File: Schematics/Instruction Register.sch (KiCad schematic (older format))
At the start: 44 parts, among them U44 74F157, U45 74F157, U46 74F574, U47 74F157, U48 74F157, U49 74F574

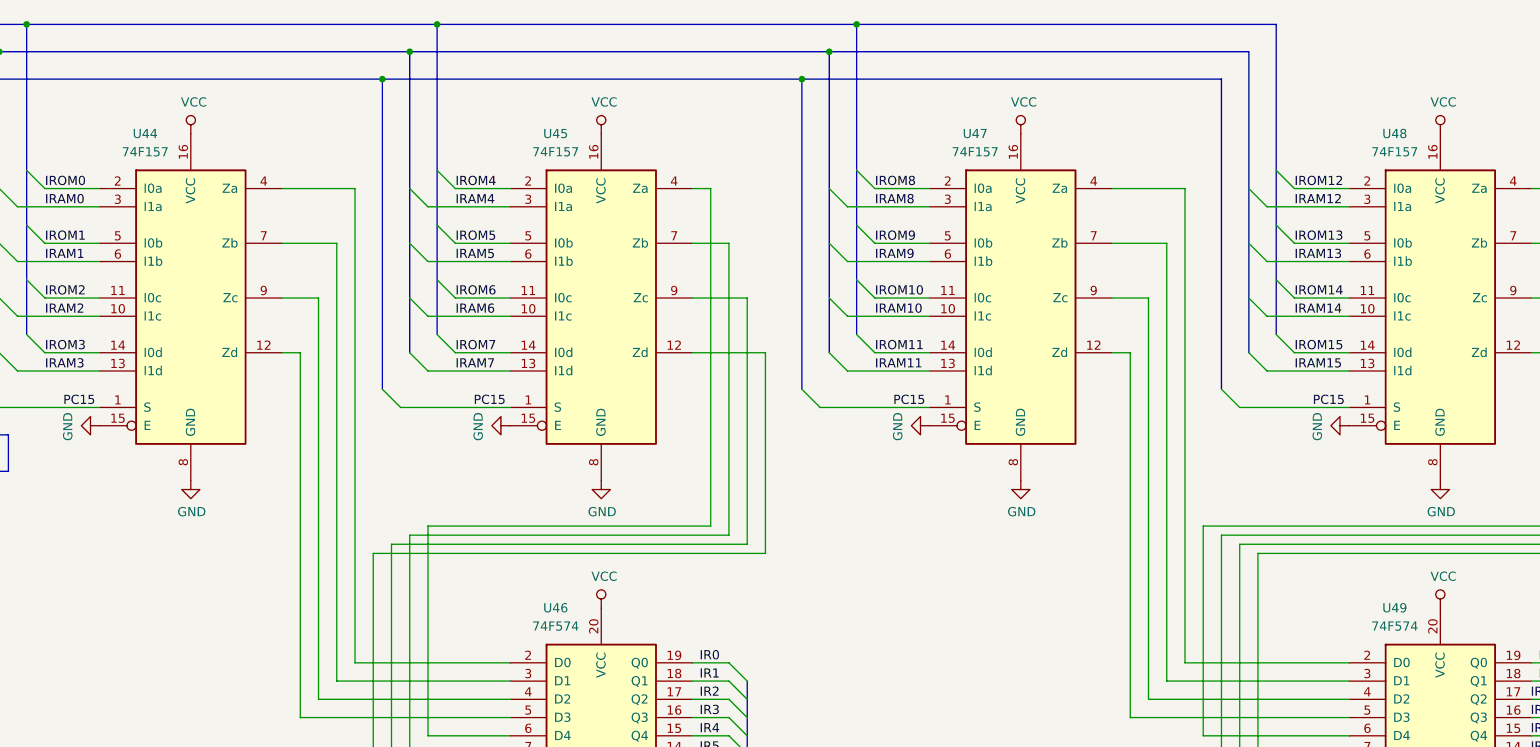
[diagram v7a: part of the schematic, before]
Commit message: Loosely group PCB footprints according to corresponding sheet.
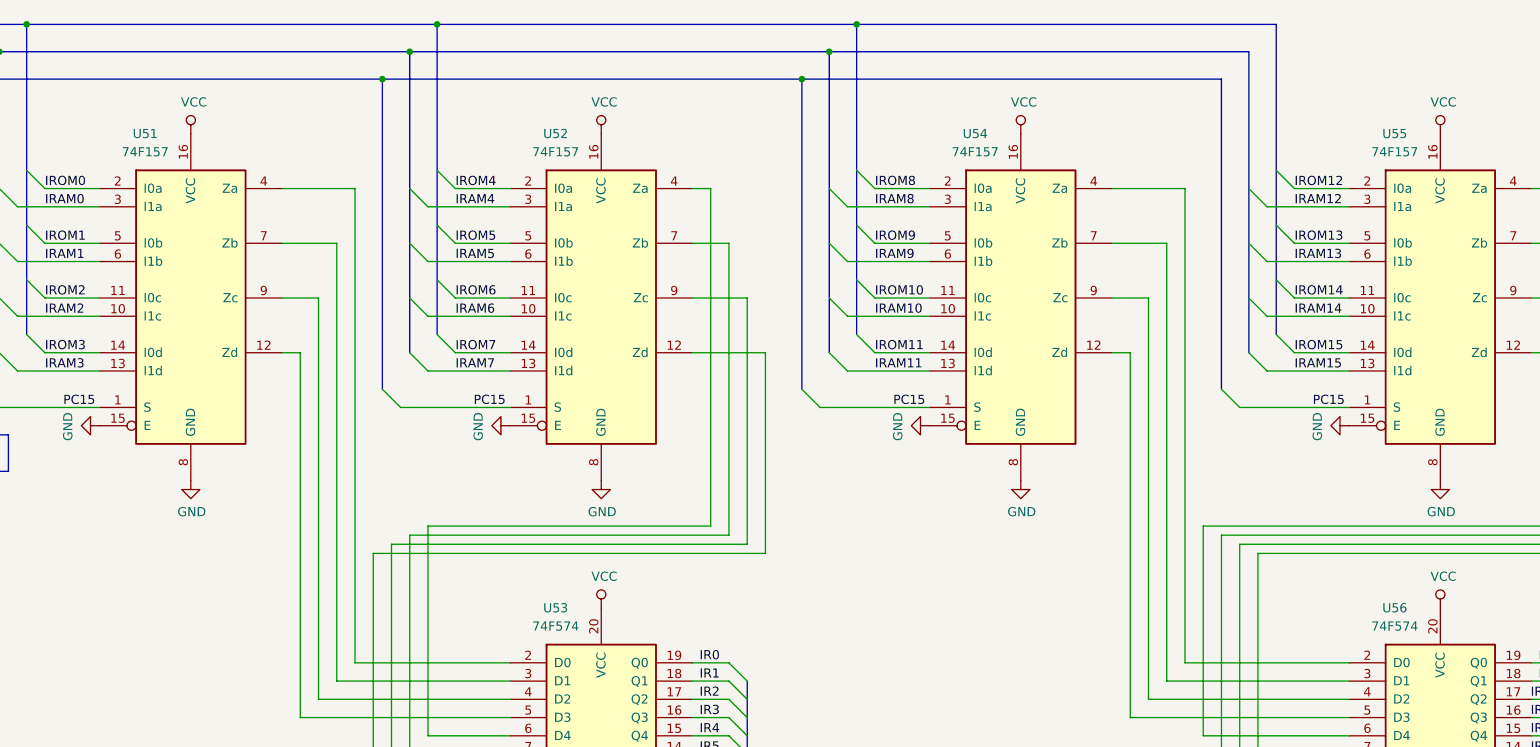
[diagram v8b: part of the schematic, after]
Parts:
- renumbered U44 to U51, U45 to U52, U46 to U53, U47 to U54, U48 to U55, U49 to U56
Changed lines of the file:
@@
 P 2100 2100
 AR Path="/5D2C14C3/5D23E2DA" Ref="U?"  Part="1"
-AR Path="/5D8005AF/5D833E49/5D23E2DA" Ref="U44"  Part="1"
-F 0 "U44" H 1850 3000 50  0000 C CNN
+AR Path="/5D8005AF/5D833E49/5D23E2DA" Ref="U51"  Part="1"
+F 0 "U51" H 1850 3000 50  0000 C CNN
 F 1 "74F157" H 1850 2900 50  0000 C CNN
 F 2 "Package_DIP:DIP-16_W7.62mm" H 2100 2100 50  0001 C CNN
@@
 P 4350 4600
 AR Path="/5D2C14C3/5D25C885" Ref="U?"  Part="1"
-AR Path="/5D8005AF/5D833E49/5D25C885" Ref="U46"  Part="1"
-F 0 "U46" H 4100 5400 50  0000 C CNN
+AR Path="/5D8005AF/5D833E49/5D25C885" Ref="U53"  Part="1"
+F 0 "U53" H 4100 5400 50  0000 C CNN
 F 1 "74F574" H 4100 5300 50  0000 C CNN
 F 2 "Package_DIP:DIP-20_W7.62mm" H 4350 4600 50  0001 C CNN
@@
 P 8950 4600
 AR Path="/5D2C14C3/5D26023C" Ref="U?"  Part="1"
-AR Path="/5D8005AF/5D833E49/5D26023C" Ref="U49"  Part="1"
-F 0 "U49" H 8700 5400 50  0000 C CNN
+AR Path="/5D8005AF/5D833E49/5D26023C" Ref="U56"  Part="1"
+F 0 "U56" H 8700 5400 50  0000 C CNN
 F 1 "74F574" H 8700 5300 50  0000 C CNN
 F 2 "Package_DIP:DIP-20_W7.62mm" H 8950 4600 50  0001 C CNN
@@
 P 4350 2100
 AR Path="/5D2C14C3/5D24114A" Ref="U?"  Part="1"
-AR Path="/5D8005AF/5D833E49/5D24114A" Ref="U45"  Part="1"
-F 0 "U45" H 4100 3000 50  0000 C CNN
+AR Path="/5D8005AF/5D833E49/5D24114A" Ref="U52"  Part="1"
+F 0 "U52" H 4100 3000 50  0000 C CNN
 F 1 "74F157" H 4100 2900 50  0000 C CNN
 F 2 "Package_DIP:DIP-16_W7.62mm" H 4350 2100 50  0001 C CNN
@@
 P 6650 2100
 AR Path="/5D2C14C3/5DA1424F" Ref="U?"  Part="1"
-AR Path="/5D8005AF/5D833E49/5DA1424F" Ref="U47"  Part="1"
-F 0 "U47" H 6400 3000 50  0000 C CNN
+AR Path="/5D8005AF/5D833E49/5DA1424F" Ref="U54"  Part="1"
+F 0 "U54" H 6400 3000 50  0000 C CNN
 F 1 "74F157" H 6400 2900 50  0000 C CNN
 F 2 "Package_DIP:DIP-16_W7.62mm" H 6650 2100 50  0001 C CNN
@@
 P 8950 2100
 AR Path="/5D2C14C3/5DA1933F" Ref="U?"  Part="1"
-AR Path="/5D8005AF/5D833E49/5DA1933F" Ref="U48"  Part="1"
-F 0 "U48" H 8700 3000 50  0000 C CNN
+AR Path="/5D8005AF/5D833E49/5DA1933F" Ref="U55"  Part="1"
+F 0 "U55" H 8700 3000 50  0000 C CNN
 F 1 "74F157" H 8700 2900 50  0000 C CNN
 F 2 "Package_DIP:DIP-16_W7.62mm" H 8950 2100 50  0001 C CNN
